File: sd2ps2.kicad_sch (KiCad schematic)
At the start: 9 parts, among them J1 , J2 DM3AT-SF-PEJM5, Q1 DTC114T, Q2 DTC114T

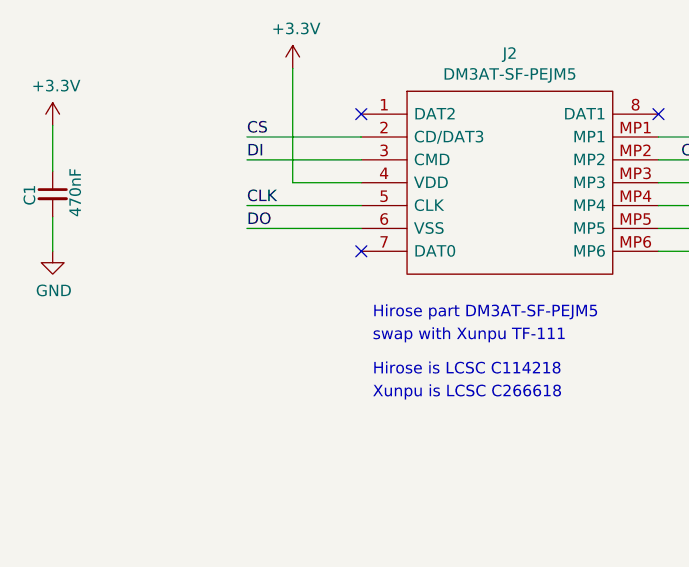
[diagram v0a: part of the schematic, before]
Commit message: Fix VSS-D0 pin snafu
I misread the instructions on the tin. Ground is important.

also clean up some things that git doesn't need to know about in kicad's world
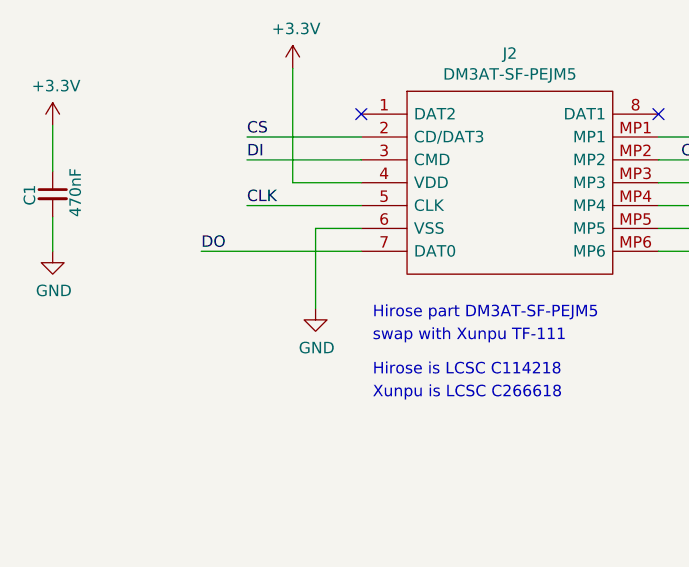
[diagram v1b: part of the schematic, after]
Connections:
- net DO: now also J2.7 (DAT0); no longer J2.6 (VSS)
- net GND: now also J2.6 (VSS)
- no-connect marks 4 -> 3
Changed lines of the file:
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@@
   (no_connect (at 106.68 102.87))
   (no_connect (at 96.52 74.93))
-  (no_connect (at 106.68 118.11))
   (no_connect (at 139.7 102.87))
   (wire (pts (xy 156.21 46.99) (xy 156.21 54.61))
@@
     (stroke (width 0) (type default) (color 0 0 0 0))
   )
+  (wire (pts (xy 101.6 115.57) (xy 101.6 124.46))
+    (stroke (width 0) (type default) (color 0 0 0 0))
+  )
   (wire (pts (xy 96.52 69.85) (xy 104.14 69.85))
     (stroke (width 0) (type default) (color 0 0 0 0))
@@
     (stroke (width 0) (type default) (color 0 0 0 0))
   )
-  (wire (pts (xy 93.98 115.57) (xy 106.68 115.57))
+  (wire (pts (xy 88.9 118.11) (xy 106.68 118.11))
     (stroke (width 0) (type default) (color 0 0 0 0))
   )
@@
   )
   (wire (pts (xy 198.12 90.17) (xy 200.66 90.17))
+    (stroke (width 0) (type default) (color 0 0 0 0))
+  )
+  (wire (pts (xy 106.68 115.57) (xy 101.6 115.57))
     (stroke (width 0) (type default) (color 0 0 0 0))
   )
@@
     (effects (font (size 1.27 1.27)) (justify right bottom))
   )
-  (label "DO" (at 93.98 115.57 0)
+  (label "DO" (at 88.9 118.11 0)
     (effects (font (size 1.27 1.27)) (justify left bottom))
   )
@@
     (pin "3")
   )
+  (symbol (lib_id "power:GND") (at 101.6 124.46 0) (unit 1)
+    (in_bom yes) (on_board yes)
+    (property "Reference" "#PWR0101" (id 0) (at 101.6 130.81 0)
+      (effects (font (size 1.27 1.27)) hide)
+    )
+    (property "Value" "GND" (id 1) (at 101.727 128.8542 0))
+    (property "Footprint" "" (id 2) (at 101.6 124.46 0)
+      (effects (font (size 1.27 1.27)) hide)
+    )
+    (property "Datasheet" "" (id 3) (at 101.6 124.46 0)
+      (effects (font (size 1.27 1.27)) hide)
+    )
+    (pin "1")
+  )
   (sheet_instances
     (path "/" (page "1"))
@@
       (reference "#PWR011") (unit 1) (value "GND") (footprint "")
     )
+    (path "/ca4eb899-5545-4f19-9fd0-836b2d42f0d7"
+      (reference "#PWR0101") (unit 1) (value "GND") (footprint "")
+    )
     (path "/00000000-0000-0000-0000-000061fce1c2"

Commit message: rev b
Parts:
- removed LED1: LTST-S327KGKFKT, LTSTS327KGKFKT, symbol local:LTST-S327KGKFKT
- removed R2, R3: 1K, Resistor_SMD:R_1206_3216Metric, symbol Device:R
- added LED1: LTST-S270KGKT, LTSTS270KRKT, symbol local:LTST-S270KGKT
- added LED2: LTST-S270KRKT, LTSTS270KRKT, symbol local:LTST-S270KRKT
- added RN1, RN2: CAY16-1002F4LF, Resistor_SMD:R_Array_Convex_4x1206, symbol local:CAY16-1002F4LF
- J1, R1: now left out of the parts list
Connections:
- net +3V3: now also RN1.1, RN1.2, RN1.3, RN1.4
- net CD: now also RN2.1, RN2.2
- net CS: now also RN1.7
- net DO: now also RN1.6
- net GND: now also LED1.1, LED2.1
- net at Q2.2 (E): now also RN2.3, RN2.4
- net at J2.1 (DAT2): now also RN1.8
- net at J2.8 (DAT1): now also RN1.5
- new net: LED1.2, RN2.5, RN2.6
- new net: LED2.2, RN2.7, RN2.8
- no-connect marks 3 -> 1
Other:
- note added: "NO STUFF"
- moved on the sheet: Q2

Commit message: update tweaks
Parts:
- added FID1, FID2: Fiducial, Fiducial:Fiducial_0.75mm_Mask1.5mm, symbol Mechanical:Fiducial
- added FID3: Fiducial, Fiducial:Fiducial_1mm_Mask2mm, symbol Mechanical:Fiducial
- LED1, LED2: footprint LTSTS270KRKT -> sd2ps2:LTSTS270KxKT
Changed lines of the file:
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@@
   (junction (at 175.26 91.44) (diameter 0) (color 0 0 0 0)
   )
-  (junction (at 142.24 93.98) (diameter 0) (color 0 0 0 0)
-  )
   (junction (at 144.78 74.93) (diameter 0) (color 0 0 0 0)
   )
@@
   )
   (junction (at 146.05 115.57) (diameter 0) (color 0 0 0 0)
-  )
-  (junction (at 144.78 59.69) (diameter 0) (color 0 0 0 0)
   )
   (junction (at 146.05 110.49) (diameter 0) (color 0 0 0 0)
@@
     (stroke (width 0) (type default) (color 0 0 0 0))
   )
-  (wire (pts (xy 139.7 59.69) (xy 144.78 59.69))
-    (stroke (width 0) (type default) (color 0 0 0 0))
-  )
   (wire (pts (xy 173.99 74.93) (xy 173.99 77.47))
     (stroke (width 0) (type default) (color 0 0 0 0))
@@
   )
   (wire (pts (xy 80.01 96.52) (xy 82.55 96.52))
-    (stroke (width 0) (type default) (color 0 0 0 0))
-  )
-  (wire (pts (xy 142.24 93.98) (xy 144.78 93.98))
     (stroke (width 0) (type default) (color 0 0 0 0))
   )
@@
   (label "CD" (at 144.78 107.95 180)
     (effects (font (size 1.27 1.27)) (justify right bottom))
-  )
-  (label "CD" (at 139.7 59.69 0)
-    (effects (font (size 1.27 1.27)) (justify left bottom))
   )
   (label "CS" (at 113.03 67.31 180)
@@
       (effects (font (size 1.27 1.27)) (justify right))
     )
-    (property "Footprint" "LTSTS270KRKT" (id 2) (at 160.02 97.79 0)
+    (property "Footprint" "sd2ps2:LTSTS270KxKT" (id 2) (at 160.02 97.79 0)
       (effects (font (size 1.27 1.27)) (justify left bottom) hide)
     )
@@
     (pin "1")
     (pin "2")
+  )
+  (symbol (lib_id "Mechanical:Fiducial") (at 198.12 128.27 0) (unit 1)
+    (in_bom no) (on_board yes) (fields_autoplaced)
+    (property "Reference" "FID3" (id 0) (at 200.279 127.3615 0)
+      (effects (font (size 1.27 1.27)) (justify left))
+    )
+    (property "Value" "Fiducial" (id 1) (at 200.279 130.1366 0)
+      (effects (font (size 1.27 1.27)) (justify left))
+    )
+    (property "Footprint" "Fiducial:Fiducial_1mm_Mask2mm" (id 2) (at 198.12 128.27 0)
+      (effects (font (size 1.27 1.27)) hide)
+    )
+    (property "Datasheet" "~" (id 3) (at 198.12 128.27 0)
+      (effects (font (size 1.27 1.27)) hide)
+    )
+  )
+  (symbol (lib_id "Mechanical:Fiducial") (at 198.12 118.11 0) (unit 1)
+    (in_bom no) (on_board yes) (fields_autoplaced)
+    (property "Reference" "FID1" (id 0) (at 200.279 117.2015 0)
+      (effects (font (size 1.27 1.27)) (justify left) hide)
+    )
+    (property "Value" "Fiducial" (id 1) (at 200.279 118.589 0)
+      (effects (font (size 1.27 1.27)) (justify left))
+    )
+    (property "Footprint" "Fiducial:Fiducial_0.75mm_Mask1.5mm" (id 2) (at 198.12 118.11 0)
+      (effects (font (size 1.27 1.27)) hide)
+    )
+    (property "Datasheet" "~" (id 3) (at 198.12 118.11 0)
+      (effects (font (size 1.27 1.27)) hide)
+    )
   )
   (symbol (lib_id "local:CAY16-1002F4LF") (at 80.01 90.17 0) (unit 1)
@@
     (pin "8")
   )
+  (symbol (lib_id "Mechanical:Fiducial") (at 198.12 123.19 0) (unit 1)
+    (in_bom no) (on_board yes) (fields_autoplaced)
+    (property "Reference" "FID2" (id 0) (at 200.279 122.2815 0)
+      (effects (font (size 1.27 1.27)) (justify left))
+    )
+    (property "Value" "Fiducial" (id 1) (at 200.279 125.0566 0)
+      (effects (font (size 1.27 1.27)) (justify left))
+    )
+    (property "Footprint" "Fiducial:Fiducial_0.75mm_Mask1.5mm" (id 2) (at 198.12 123.19 0)
+      (effects (font (size 1.27 1.27)) hide)
+    )
+    (property "Datasheet" "~" (id 3) (at 198.12 123.19 0)
+      (effects (font (size 1.27 1.27)) hide)
+    )
+  )
   (symbol (lib_id "local:LTST-S270KRKT") (at 181.61 110.49 90) (unit 1)
     (in_bom yes) (on_board yes) (fields_autoplaced)
@@
       (effects (font (size 1.27 1.27)) (justify right))
     )
-    (property "Footprint" "LTSTS270KRKT" (id 2) (at 177.8 97.79 0)
+    (property "Footprint" "sd2ps2:LTSTS270KxKT" (id 2) (at 177.8 97.79 0)
       (effects (font (size 1.27 1.27)) (justify left bottom) hide)
     )
@@
       (reference "C1") (unit 1) (value "470nF") (footprint "Capacitor_SMD:C_1206_3216Metric")
     )
+    (path "/2fb045bf-18db-49ea-b1e6-b2c67e776cd6"
+      (reference "FID1") (unit 1) (value "Fiducial") (footprint "Fiducial:Fiducial_0.75mm_Mask1.5mm")
+    )
+    (path "/36ff8212-16d0-4721-984b-0554cfc79b2f"
+      (reference "FID2") (unit 1) (value "Fiducial") (footprint "Fiducial:Fiducial_0.75mm_Mask1.5mm")
+    )
+    (path "/28812fda-e63a-4d05-8523-c525b1073492"
+      (reference "FID3") (unit 1) (value "Fiducial") (footprint "Fiducial:Fiducial_1mm_Mask2mm")
+    )
     (path "/00000000-0000-0000-0000-000061f8c114"
       (reference "J1") (unit 1) (value " ") (footprint "sd2ps2:PlayStation_Memory_Card")
@@
     )
     (path "/1ffb232f-c2ec-4701-90b0-019b420fec65"
-      (reference "LED1") (unit 1) (value "LTST-S270KGKT") (footprint "LTSTS270KRKT")
+      (reference "LED1") (unit 1) (value "LTST-S270KGKT") (footprint "sd2ps2:LTSTS270KxKT")
     )
     (path "/ac8b06a8-9d55-4897-b534-bfecaf7772a4"
-      (reference "LED2") (unit 1) (value "LTST-S270KRKT") (footprint "LTSTS270KRKT")
+      (reference "LED2") (unit 1) (value "LTST-S270KRKT") (footprint "sd2ps2:LTSTS270KxKT")
     )
     (path "/00000000-0000-0000-0000-000062115cbf"
